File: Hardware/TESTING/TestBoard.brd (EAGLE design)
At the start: 116.8 x 44.5 mm, 102 parts, among them IC1 OP-AMP, U1 TAP_POINT, U10 MCP1755, U11 AD7280A, U2 TAP_POINT, U3 TAP_POINT, U4 TAP_POINT, U5 TAP_POINT

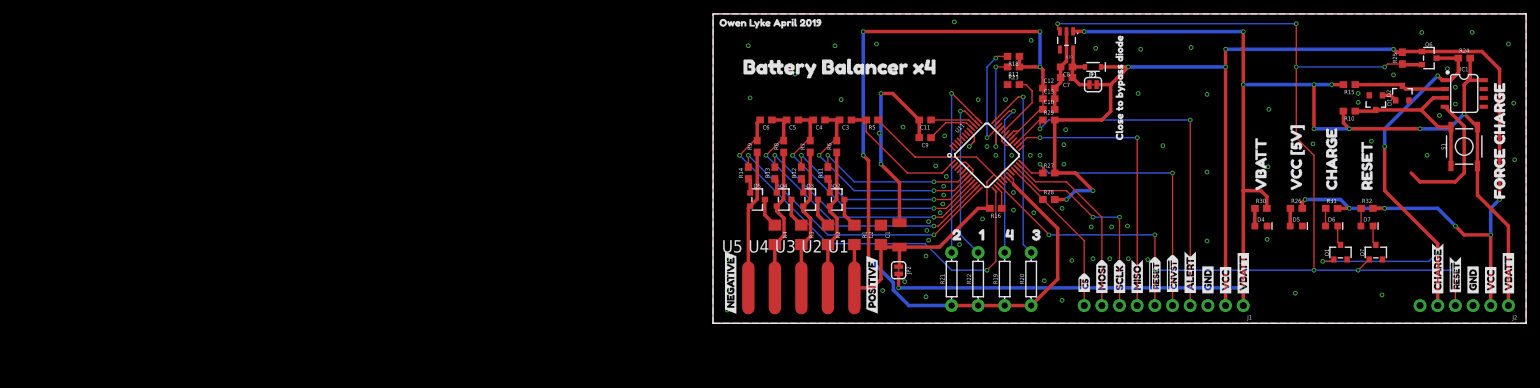
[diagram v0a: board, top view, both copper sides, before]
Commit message: Gerbered the testing board
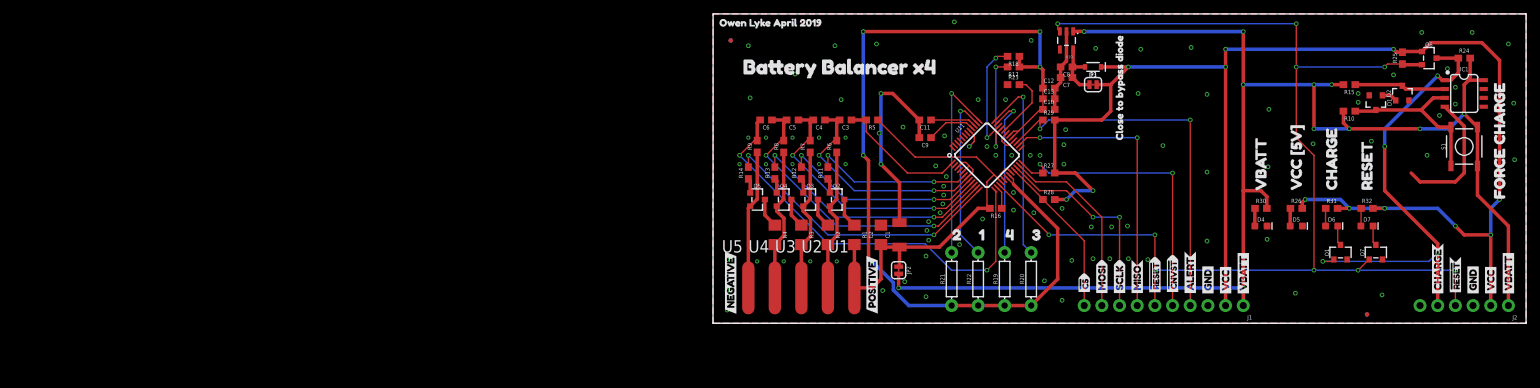
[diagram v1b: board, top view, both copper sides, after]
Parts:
- added FD1, FD2, FD3, FD4: FIDUCIALUFIDUCIAL, SparkFun-Aesthetics:FIDUCIAL-MICRO
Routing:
- net VCC: track 201.7 -> 203.5 mm
- net GND: vias 83 -> 96
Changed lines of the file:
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@@
 <?xml version="1.0" encoding="utf-8"?>
 <!DOCTYPE eagle SYSTEM "eagle.dtd">
-<eagle version="9.2.0">
+<eagle version="9.1.3">
 <drawing>
 <settings>
-<setting alwaysvectorfont="no"/>
+<setting alwaysvectorfont="yes"/>
 <setting verticaltext="up"/>
 </settings>
-<grid distance="0.05" unitdist="inch" unit="inch" style="lines" multiple="1" display="yes" altdistance="0.005" altunitdist="inch" altunit="inch"/>
+<grid distance="50" unitdist="mil" unit="mil" style="lines" multiple="1" display="yes" altdistance="1" altunitdist="mil" altunit="mil"/>
 <layers>
 <layer number="1" name="Top" color="4" fill="1" visible="yes" active="yes"/>
@@
 <layer number="23" name="tOrigins" color="15" fill="1" visible="yes" active="yes"/>
 <layer number="24" name="bOrigins" color="15" fill="1" visible="yes" active="yes"/>
-<layer number="25" name="tNames" color="7" fill="1" visible="yes" active="yes"/>
-<layer number="26" name="bNames" color="7" fill="1" visible="yes" active="yes"/>
-<layer number="27" name="tValues" color="7" fill="1" visible="yes" active="yes"/>
-<layer number="28" name="bValues" color="7" fill="1" visible="yes" active="yes"/>
-<layer number="29" name="tStop" color="7" fill="3" visible="yes" active="yes"/>
-<layer number="30" name="bStop" color="7" fill="6" visible="yes" active="yes"/>
-<layer number="31" name="tCream" color="7" fill="4" visible="yes" active="yes"/>
-<layer number="32" name="bCream" color="7" fill="5" visible="yes" active="yes"/>
-<layer number="33" name="tFinish" color="6" fill="3" visible="yes" active="yes"/>
-<layer number="34" name="bFinish" color="6" fill="6" visible="yes" active="yes"/>
-<layer number="35" name="tGlue" color="7" fill="4" visible="yes" active="yes"/>
-<layer number="36" name="bGlue" color="7" fill="5" visible="yes" active="yes"/>
-<layer number="37" name="tTest" color="7" fill="1" visible="yes" active="yes"/>
-<layer number="38" name="bTest" color="7" fill="1" visible="yes" active="yes"/>
-<layer number="39" name="tKeepout" color="4" fill="11" visible="yes" active="yes"/>
-<layer number="40" name="bKeepout" color="1" fill="11" visible="yes" active="yes"/>
-<layer number="41" name="tRestrict" color="4" fill="10" visible="yes" active="yes"/>
-<layer number="42" name="bRestrict" color="1" fill="10" visible="yes" active="yes"/>
-<layer number="43" name="vRestrict" color="2" fill="10" visible="yes" active="yes"/>
-<layer number="44" name="Drills" color="7" fill="1" visible="yes" active="yes"/>
+<layer number="25" name="tNames" color="7" fill="1" visible="no" active="yes"/>
+<layer number="26" name="bNames" color="7" fill="1" visible="no" active="yes"/>
+<layer number="27" name="tValues" color="7" fill="1" visible="no" active="yes"/>
+<layer number="28" name="bValues" color="7" fill="1" visible="no" active="yes"/>
+<layer number="29" name="tStop" color="7" fill="3" visible="no" active="yes"/>
+<layer number="30" name="bStop" color="7" fill="6" visible="no" active="yes"/>
+<layer number="31" name="tCream" color="7" fill="4" visible="no" active="yes"/>
+<layer number="32" name="bCream" color="7" fill="5" visible="no" active="yes"/>
+<layer number="33" name="tFinish" color="6" fill="3" visible="no" active="yes"/>
+<layer number="34" name="bFinish" color="6" fill="6" visible="no" active="yes"/>
+<layer number="35" name="tGlue" color="7" fill="4" visible="no" active="yes"/>
+<layer number="36" name="bGlue" color="7" fill="5" visible="no" active="yes"/>
+<layer number="37" name="tTest" color="7" fill="1" visible="no" active="yes"/>
+<layer number="38" name="bTest" color="7" fill="1" visible="no" active="yes"/>
+<layer number="39" name="tKeepout" color="4" fill="11" visible="no" active="yes"/>
+<layer number="40" name="bKeepout" color="1" fill="11" visible="no" active="yes"/>
+<layer number="41" name="tRestrict" color="4" fill="10" visible="no" active="yes"/>
+<layer number="42" name="bRestrict" color="1" fill="10" visible="no" active="yes"/>
+<layer number="43" name="vRestrict" color="2" fill="10" visible="no" active="yes"/>
+<layer number="44" name="Drills" color="7" fill="1" visible="no" active="yes"/>
 <layer number="45" name="Holes" color="7" fill="1" visible="yes" active="yes"/>
-<layer number="46" name="Milling" color="3" fill="1" visible="yes" active="yes"/>
-<layer number="47" name="Measures" color="7" fill="1" visible="yes" active="yes"/>
-<layer number="48" name="Document" color="7" fill="1" visible="yes" active="yes"/>
-<layer number="49" name="Reference" color="7" fill="1" visible="yes" active="yes"/>
-<layer number="50" name="dxf" color="7" fill="1" visible="yes" active="yes"/>
+<layer number="46" name="Milling" color="3" fill="1" visible="no" active="yes"/>
+<layer number="47" name="Measures" color="7" fill="1" visible="no" active="yes"/>
+<layer number="48" name="Document" color="7" fill="1" visible="no" active="yes"/>
+<layer number="49" name="Reference" color="7" fill="1" visible="no" active="yes"/>
+<layer number="50" name="dxf" color="7" fill="1" visible="no" active="yes"/>
 <layer number="51" name="tDocu" color="6" fill="1" visible="yes" active="yes"/>
-<layer number="52" name="bDocu" color="7" fill="1" visible="yes" active="yes"/>
+<layer number="52" name="bDocu" color="7" fill="1" visible="no" active="yes"/>
 <layer number="91" name="Nets" color="2" fill="1" visible="no" active="no"/>
 <layer number="92" name="Busses" color="1" fill="1" visible="no" active="no"/>
@@
 <layer number="95" name="Names" color="7" fill="1" visible="no" active="no"/>
 <layer number="96" name="Values" color="7" fill="1" visible="no" active="no"/>
-<layer number="2" name="Route2" color="16" fill="1" visible="yes" active="yes"/>
-<layer number="15" name="Route15" color="23" fill="1" visible="yes" active="yes"/>
+<layer number="2" name="Route2" color="16" fill="1" visible="no" active="no"/>
+<layer number="15" name="Route15" color="23" fill="1" visible="no" active="no"/>
 <layer number="53" name="tGND_GNDA" color="7" fill="9" visible="no" active="no"/>
 <layer number="54" name="bGND_GNDA" color="1" fill="9" visible="no" active="no"/>
@@
 <element name="U$28" library="buzzard_labels_test" package="FORCE_CHARGE20" value="" x="113.03" y="16.51" rot="R90"/>
 <element name="U$29" library="buzzard_labels_test" package="BATTERY_BALANCER_X421" value="" x="2.54" y="36.83"/>
+<element name="FD1" library="SparkFun-Aesthetics" package="FIDUCIAL-MICRO" value="FIDUCIALUFIDUCIAL" x="2.54" y="40.64"/>
+<element name="FD2" library="SparkFun-Aesthetics" package="FIDUCIAL-MICRO" value="FIDUCIALUFIDUCIAL" x="2.54" y="40.64" rot="MR0"/>
+<element name="FD3" library="SparkFun-Aesthetics" package="FIDUCIAL-MICRO" value="FIDUCIALUFIDUCIAL" x="93.98" y="1.27"/>
+<element name="FD4" library="SparkFun-Aesthetics" package="FIDUCIAL-MICRO" value="FIDUCIALUFIDUCIAL" x="93.98" y="1.27" rot="MR0"/>
 </elements>
 <signals>
@@
 <contactref element="Q7" pad="2"/>
 <contactref element="Q1" pad="2"/>
+<via x="5.08" y="26.67" extent="1-16" drill="0.3048"/>
+<via x="7.62" y="26.67" extent="1-16" drill="0.3048"/>
+<via x="11.43" y="26.67" extent="1-16" drill="0.3048"/>
+<via x="15.24" y="26.67" extent="1-16" drill="0.3048"/>
+<via x="19.05" y="26.67" extent="1-16" drill="0.3048"/>
+<via x="3.81" y="22.86" extent="1-16" drill="0.3048"/>
+<via x="7.62" y="22.86" extent="1-16" drill="0.3048"/>
+<via x="11.43" y="22.86" extent="1-16" drill="0.3048"/>
+<via x="15.24" y="22.86" extent="1-16" drill="0.3048"/>
+<via x="6.35" y="8.89" extent="1-16" drill="0.3048"/>
+<via x="10.16" y="8.89" extent="1-16" drill="0.3048"/>
+<via x="13.97" y="8.89" extent="1-16" drill="0.3048"/>
+<via x="17.78" y="8.89" extent="1-16" drill="0.3048"/>
+<wire x1="13.97" y1="8.89" x2="17.78" y2="8.89" width="0" layer="19" extent="1-1"/>
 </signal>
 <signal name="N$5">
@@
 <wire x1="111.76" y1="16.51" x2="113.03" y2="17.78" width="0.508" layer="16"/>
 <via x="113.03" y="17.78" extent="1-16" drill="0.381"/>
-<wire x1="101.87" y1="39.05" x2="110.49" y2="39.05" width="0.508" layer="1"/>
-<wire x1="110.49" y1="39.05" x2="113.03" y2="36.51" width="0.508" layer="1"/>
-<wire x1="113.03" y1="36.51" x2="113.03" y2="17.78" width="0.508" layer="1"/>
+<wire x1="103.14" y1="40.32" x2="110.49" y2="40.32" width="0.508" layer="1"/>
+<wire x1="110.49" y1="40.32" x2="113.03" y2="37.78" width="0.508" layer="1"/>
+<wire x1="113.03" y1="37.78" x2="113.03" y2="17.78" width="0.508" layer="1"/>
 <contactref element="R26" pad="2"/>
 <contactref element="R31" pad="2"/>
@@
 <wire x1="85.09" y1="17.78" x2="90.17" y2="17.78" width="0.508" layer="16"/>
 <wire x1="90.17" y1="17.78" x2="91.44" y2="16.51" width="0.508" layer="16"/>
+<wire x1="101.87" y1="39.05" x2="103.14" y2="40.32" width="0.508" layer="1"/>
 </signal>
 <signal name="N$41">
@@
 <wire x1="93.13" y1="13.997" x2="93.103" y2="13.97" width="0.2032" layer="1"/>
 </signal>
+<signal name="N$49">
+<via x="19.05" y="22.86" extent="1-16" drill="0.3048"/>
+</signal>
 </signals>

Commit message: Implement LV shutoff circuit changes in schematic
Switch to voltage-divider/zener comparator, change regulator enable to raw compararator output
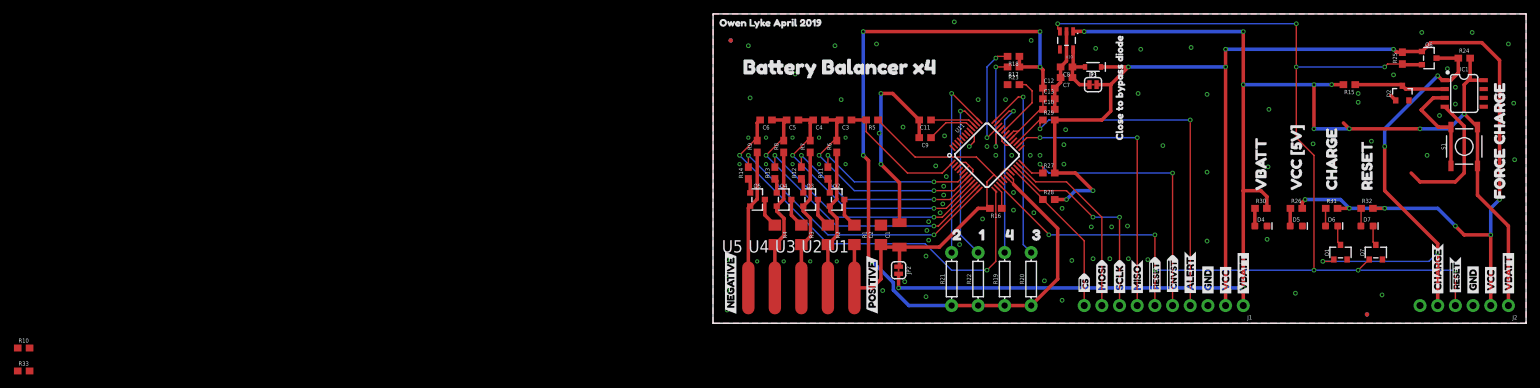
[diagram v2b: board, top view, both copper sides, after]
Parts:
- removed D1: MATCH, SparkFun-DiscreteSemi:SOT23-3
- added R33: 10M, SparkFun-Resistors:0603
- D2: value TH -> TH-12V
- R10: value 1M -> 330k
- moved R10 193.5 mm to (-99.1, -3.56), turned to 0 degrees
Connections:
- net CHARGE: now also U10.3
- net GND: now also R33.1; no longer D1.1
- net N$40: now also R33.2; no longer D1.3
- net RESET: no longer U10.3
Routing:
- net N$40: track 24.5 -> 15.0 mm
- net V_BATT: track 207.7 -> 206.0 mm
- net GND: track 92.4 -> 91.3 mm
